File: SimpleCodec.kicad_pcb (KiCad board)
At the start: 4 copper layers, 0 parts

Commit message: Schematic
Updated the power delivery module.
Other minor changes.
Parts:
- added A1: RP_PICO_2, Custom_Parts:RP_PICO_2_THT, F.Cu at (18.0, 36.9)
- added C1: 10u, Capacitor_SMD:C_1206_3216Metric, F.Cu at (84.0, 15.0)
- added C10: 1u, Capacitor_SMD:C_0805_2012Metric, F.Cu at (67.7, 80.0)
- added C11: 2.2n, Capacitor_SMD:C_0603_1608Metric, F.Cu at (42.9, 81.7)
- added C12: 2.2n, Capacitor_SMD:C_0603_1608Metric, F.Cu at (42.9, 84.2)
- added C13: 10u, Capacitor_SMD:C_1206_3216Metric, F.Cu at (72.3, 55.9)
- added C14: 10u, Capacitor_SMD:C_1206_3216Metric, F.Cu at (72.3, 59.2)
- added C15: 4.7u, Capacitor_SMD:C_1206_3216Metric, F.Cu at (72.3, 62.5)
- added C16: 4.7u, Capacitor_SMD:C_1206_3216Metric, F.Cu at (72.3, 65.9)
- added C17: 100n, Capacitor_SMD:C_0603_1608Metric, F.Cu at (42.9, 86.8)
- added C18: 100n, Capacitor_SMD:C_0603_1608Metric, F.Cu at (47.0, 76.7)
- added C19: 4.7u, Capacitor_SMD:C_1206_3216Metric, F.Cu at (72.3, 15.0)
- added C2: 10u, Capacitor_SMD:C_1206_3216Metric, F.Cu at (84.0, 18.4)
- added C20: 4.7u, Capacitor_SMD:C_1206_3216Metric, F.Cu at (72.3, 18.4)
- added C21: 4.7u, Capacitor_SMD:C_1206_3216Metric, F.Cu at (72.3, 21.7)
- added C22: 4.7u, Capacitor_SMD:C_1206_3216Metric, F.Cu at (72.3, 25.1)
- added C23: 68p, Capacitor_SMD:C_0603_1608Metric, F.Cu at (42.9, 35.9)
- added C24: 68p, Capacitor_SMD:C_0603_1608Metric, F.Cu at (42.9, 38.4)
- added C25: 68p, Capacitor_SMD:C_0603_1608Metric, F.Cu at (42.9, 40.9)
- added C26: 68p, Capacitor_SMD:C_0603_1608Metric, F.Cu at (42.9, 43.4)
- added C27: 4.7u, Capacitor_SMD:C_1206_3216Metric, F.Cu at (72.3, 28.4)
- added C28: 4.7u, Capacitor_SMD:C_1206_3216Metric, F.Cu at (72.3, 31.8)
- added C29: 1n, Capacitor_SMD:C_0603_1608Metric, F.Cu at (42.9, 45.9)
- added C3: 10u, Capacitor_SMD:C_1206_3216Metric, F.Cu at (84.0, 21.7)
- added C30: 1n, Capacitor_SMD:C_0603_1608Metric, F.Cu at (42.9, 48.4)
- added C31: 100n, Capacitor_SMD:C_0603_1608Metric, F.Cu at (42.9, 50.9)
- added C32: 100n, Capacitor_SMD:C_0603_1608Metric, F.Cu at (47.0, 35.9)
- added C33: 4.7u, Capacitor_SMD:C_1206_3216Metric, F.Cu at (84.0, 55.9)
- added C34: 4.7u, Capacitor_SMD:C_1206_3216Metric, F.Cu at (84.0, 59.2)
- added C35: 100n, Capacitor_SMD:C_0603_1608Metric, F.Cu at (79.2, 55.4)
- added C36: 10u, Capacitor_SMD:C_1206_3216Metric, F.Cu at (84.0, 62.5)
- added C37: 1u, Capacitor_SMD:C_0805_2012Metric, F.Cu at (89.0, 62.0)
- added C38: 1u, Capacitor_SMD:C_0805_2012Metric, F.Cu at (89.0, 65.0)
- added C39: 10u, Capacitor_SMD:C_1206_3216Metric, F.Cu at (84.0, 65.9)
- added C4: 100n, Capacitor_SMD:C_0603_1608Metric, F.Cu at (79.2, 14.6)
- added C40: 100n, Capacitor_SMD:C_0603_1608Metric, F.Cu at (79.2, 57.9)
- added C41: 10u, Capacitor_SMD:C_1206_3216Metric, F.Cu at (84.0, 69.2)
- added C42: 100n, Capacitor_SMD:C_0603_1608Metric, F.Cu at (79.2, 60.5)
- added C7: 470p, Capacitor_SMD:C_0603_1608Metric, F.Cu at (42.9, 76.7)
- added C8: 470p, Capacitor_SMD:C_0603_1608Metric, F.Cu at (42.9, 79.2)
- added C9: 1u, Capacitor_SMD:C_0805_2012Metric, F.Cu at (67.7, 77.0)
- added J1: NMJ6HCD2, Custom_Parts:NMJ6HCD2_BORDER, F.Cu at (48.8, 56.7)
- added J2: NMJ6HCD2, Custom_Parts:NMJ6HCD2_BORDER, F.Cu at (48.8, 15.8)
- added Q1: AO3401A, Package_TO_SOT_SMD:SOT-23, F.Cu at (93.5, 25.6)
- added R1: 100K, Resistor_SMD:R_0603_1608Metric, F.Cu at (79.2, 17.1)
- added R10: 100K, Resistor_SMD:R_0603_1608Metric, F.Cu at (51.0, 79.2)
- added R11: 1K, Resistor_SMD:R_0603_1608Metric, F.Cu at (51.0, 81.7)
- added R12: 1K, Resistor_SMD:R_0603_1608Metric, F.Cu at (51.0, 84.2)
- added R13: 1K, Resistor_SMD:R_0603_1608Metric, F.Cu at (51.0, 86.8)
- added R14: 1K, Resistor_SMD:R_0603_1608Metric, F.Cu at (55.0, 76.7)
- added R15: 10K, Resistor_SMD:R_0603_1608Metric, F.Cu at (55.0, 79.2)
- added R16: 10K, Resistor_SMD:R_0603_1608Metric, F.Cu at (55.0, 81.7)
- added R17: 1K, Resistor_SMD:R_0603_1608Metric, F.Cu at (55.0, 84.2)
- added R18: 1K, Resistor_SMD:R_0603_1608Metric, F.Cu at (55.0, 86.8)
- added R19: 100K, Resistor_SMD:R_0603_1608Metric, F.Cu at (47.0, 38.4)
- added R2: 10K, Resistor_SMD:R_0603_1608Metric, F.Cu at (79.2, 19.6)
- added R20: 100K, Resistor_SMD:R_0603_1608Metric, F.Cu at (47.0, 40.9)
- added R21: 100K, Resistor_SMD:R_0603_1608Metric, F.Cu at (47.0, 43.4)
- added R22: 100K, Resistor_SMD:R_0603_1608Metric, F.Cu at (47.0, 45.9)
- added R23: 12K, Resistor_SMD:R_0603_1608Metric, F.Cu at (47.0, 48.4)
- added R24: 12K, Resistor_SMD:R_0603_1608Metric, F.Cu at (47.0, 50.9)
- added R25: 12K, Resistor_SMD:R_0603_1608Metric, F.Cu at (51.0, 35.9)
- added R26: 12K, Resistor_SMD:R_0603_1608Metric, F.Cu at (51.0, 38.4)
- added R27: 22K, Resistor_SMD:R_0603_1608Metric, F.Cu at (51.0, 40.9)
- added R28: 22K, Resistor_SMD:R_0603_1608Metric, F.Cu at (51.0, 43.4)
- added R29: 22K, Resistor_SMD:R_0603_1608Metric, F.Cu at (51.0, 45.9)
- added R3: 4.7K, Resistor_SMD:R_0603_1608Metric, F.Cu at (79.2, 22.1)
- added R30: 22K, Resistor_SMD:R_0603_1608Metric, F.Cu at (51.0, 48.4)
- added R31: 220, Resistor_SMD:R_0603_1608Metric, F.Cu at (51.0, 50.9)
- added R32: 220, Resistor_SMD:R_0603_1608Metric, F.Cu at (55.0, 35.9)
- added R33: 100, Resistor_SMD:R_0603_1608Metric, F.Cu at (55.0, 38.4)
- added R34: 100, Resistor_SMD:R_0603_1608Metric, F.Cu at (55.0, 40.9)
- added R35: 47K, Resistor_SMD:R_0603_1608Metric, F.Cu at (55.0, 43.4)
- added R36: 47K, Resistor_SMD:R_0603_1608Metric, F.Cu at (55.0, 45.9)
- added R37: 47K, Resistor_SMD:R_0603_1608Metric, F.Cu at (79.2, 63.0)
- added R38: 47K, Resistor_SMD:R_0603_1608Metric, F.Cu at (79.2, 65.5)
- added R39: 47K, Resistor_SMD:R_0603_1608Metric, F.Cu at (79.2, 68.0)
- added R4: 4.7K, Resistor_SMD:R_0603_1608Metric, F.Cu at (79.2, 24.6)
- added R40: 47K, Resistor_SMD:R_0603_1608Metric, F.Cu at (79.2, 70.5)
- added R41: 47K, Resistor_SMD:R_0603_1608Metric, F.Cu at (79.2, 73.0)
- added R42: 47K, Resistor_SMD:R_0603_1608Metric, F.Cu at (79.2, 75.5)
- added R5: 100, Resistor_SMD:R_0603_1608Metric, F.Cu at (47.0, 79.2)
- added R6: 100, Resistor_SMD:R_0603_1608Metric, F.Cu at (47.0, 81.7)
- added R7: 100K, Resistor_SMD:R_0603_1608Metric, F.Cu at (47.0, 84.2)
- added R8: 100K, Resistor_SMD:R_0603_1608Metric, F.Cu at (47.0, 86.8)
- added R9: 100K, Resistor_SMD:R_0603_1608Metric, F.Cu at (51.0, 76.7)
- added U1: NE5532, Package_SO:SOIC-8_3.9x4.9mm_P1.27mm, F.Cu at (91.0, 16.7)
- added U3: AMS1117-3.3, Package_TO_SOT_SMD:SOT-223-3_TabPin2, F.Cu at (86.1, 27.6)
- added U4: NE5532, Package_SO:SOIC-8_3.9x4.9mm_P1.27mm, F.Cu at (61.2, 78.8)
- added U5: NE5532, Package_SO:SOIC-8_3.9x4.9mm_P1.27mm, F.Cu at (61.2, 85.4)
- added U6: NE5532, Package_SO:SOIC-8_3.9x4.9mm_P1.27mm, F.Cu at (61.2, 38.0)
- added U7: NE5532, Package_SO:SOIC-8_3.9x4.9mm_P1.27mm, F.Cu at (61.2, 44.5)
- added U8: TAC5242, Custom_Parts:VQFN-24-1EP_4x4mm_P0.5mm_EP2.1x2.1mm_ThermalVias, F.Cu at (90.0, 57.3)

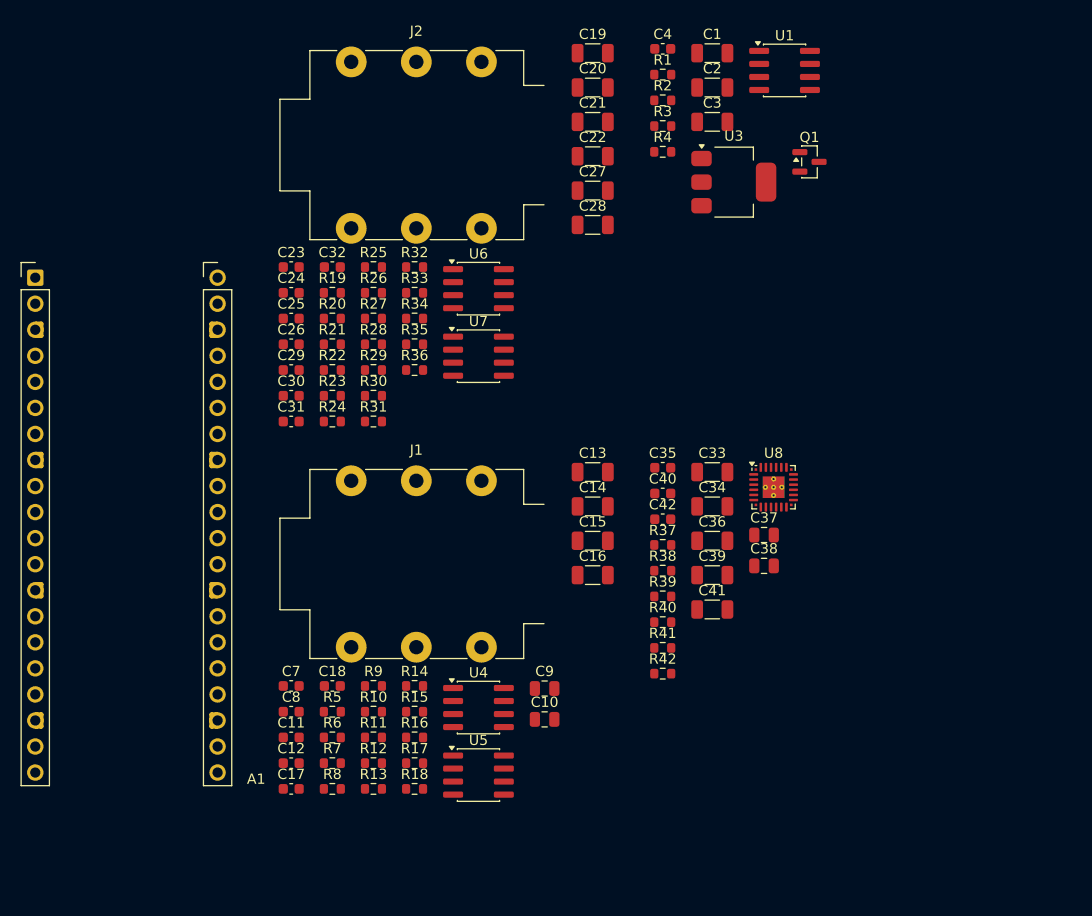
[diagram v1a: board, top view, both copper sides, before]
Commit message: Moved to a CS4272 codec as a cheaper alternative with similar performance.
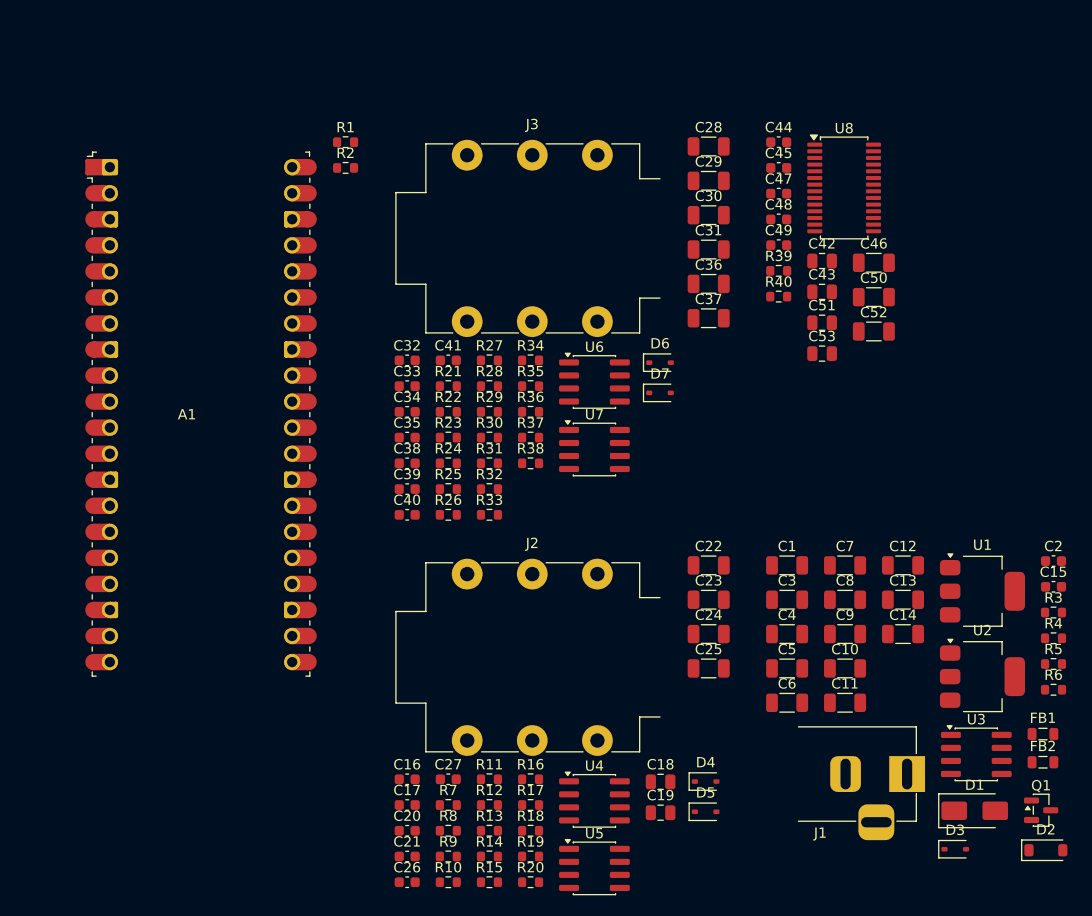
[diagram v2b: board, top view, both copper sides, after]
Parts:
- removed R41, R42: 47K, Resistor_SMD:R_0603_1608Metric
- added C43: 1u, Capacitor_SMD:C_0805_2012Metric, F.Cu at (94.7, 38.3)
- added C44: 100n, Capacitor_SMD:C_0603_1608Metric, F.Cu at (90.5, 23.7)
- added C45: 100n, Capacitor_SMD:C_0603_1608Metric, F.Cu at (90.5, 26.2)
- added C46: 4.7u, Capacitor_SMD:C_1206_3216Metric, F.Cu at (99.8, 35.4)
- added C47: 100n, Capacitor_SMD:C_0603_1608Metric, F.Cu at (90.5, 28.7)
- added C48: 100n, Capacitor_SMD:C_0603_1608Metric, F.Cu at (90.5, 31.2)
- added C49: 100n, Capacitor_SMD:C_0603_1608Metric, F.Cu at (90.5, 33.7)
- added C5: 10u, Capacitor_SMD:C_1206_3216Metric, F.Cu at (91.3, 75.0)
- added C50: 4.7u, Capacitor_SMD:C_1206_3216Metric, F.Cu at (99.8, 38.8)
- added C51: 1u, Capacitor_SMD:C_0805_2012Metric, F.Cu at (94.7, 41.3)
- added C52: 22u, Capacitor_SMD:C_1206_3216Metric, F.Cu at (99.8, 42.1)
- added C53: 1u, Capacitor_SMD:C_0805_2012Metric, F.Cu at (94.7, 44.3)
- added C6: 4.7u, Capacitor_SMD:C_1206_3216Metric, F.Cu at (91.3, 78.3)
- added D1: SMAJ10CA, Diode_SMD:D_SMA, F.Cu at (109.6, 88.9)
- added D2: MMSZ5248B, Diode_SMD:D_SOD-123, F.Cu at (116.5, 92.7)
- added D3: 1N5819WS, Diode_SMD:D_SOD-323, F.Cu at (107.7, 92.6)
- added D4: H15VSD3B, Diode_SMD:D_SOD-323, F.Cu at (83.4, 86.0)
- added D5: H15VSD3B, Diode_SMD:D_SOD-323, F.Cu at (83.4, 89.0)
- added D6: H15VSD3B, Diode_SMD:D_SOD-323, F.Cu at (78.9, 45.2)
- added D7: H15VSD3B, Diode_SMD:D_SOD-323, F.Cu at (78.9, 48.1)
- added FB1: 300, Inductor_SMD:L_0805_2012Metric, F.Cu at (116.2, 81.4)
- added FB2: 300, Inductor_SMD:L_0805_2012Metric, F.Cu at (116.2, 84.2)
- added J3: NMJ6HCD2, Custom_Parts:NMJ6HCD2_BORDER, F.Cu at (60.1, 24.9)
- added U2: AMS1117-3.3, Package_TO_SOT_SMD:SOT-223-3_TabPin2, F.Cu at (110.3, 75.8)
- A1: footprint Custom_Parts:RP_PICO_2_THT -> Custom_Parts:RP_PICO_2_SMD
- C1, C13, C3: value 10u -> 22u
- C10, C37, C9: value 1u -> 4.7u; footprint Capacitor_SMD:C_0805_2012Metric -> Capacitor_SMD:C_1206_3216Metric
- C11: value 2.2n -> 10u; footprint Capacitor_SMD:C_0603_1608Metric -> Capacitor_SMD:C_1206_3216Metric
- C12: value 2.2n -> 22u; footprint Capacitor_SMD:C_0603_1608Metric -> Capacitor_SMD:C_1206_3216Metric
- C15, C27: value 4.7u -> 100n; footprint Capacitor_SMD:C_1206_3216Metric -> Capacitor_SMD:C_0603_1608Metric
- C16: value 4.7u -> 470p; footprint Capacitor_SMD:C_1206_3216Metric -> Capacitor_SMD:C_0603_1608Metric
- C17: value 100n -> 470p
- C18, C42: value 100n -> 1u; footprint Capacitor_SMD:C_0603_1608Metric -> Capacitor_SMD:C_0805_2012Metric
- C19: value 4.7u -> 1u; footprint Capacitor_SMD:C_1206_3216Metric -> Capacitor_SMD:C_0805_2012Metric
- C2: value 10u -> 10n; footprint Capacitor_SMD:C_1206_3216Metric -> Capacitor_SMD:C_0603_1608Metric
- C20, C21: value 4.7u -> 2.2n; footprint Capacitor_SMD:C_1206_3216Metric -> Capacitor_SMD:C_0603_1608Metric
- C22: value 4.7u -> 10u
- C23: value 68p -> 10u; footprint Capacitor_SMD:C_0603_1608Metric -> Capacitor_SMD:C_1206_3216Metric
- C24, C25: value 68p -> 4.7u; footprint Capacitor_SMD:C_0603_1608Metric -> Capacitor_SMD:C_1206_3216Metric
- C26: value 68p -> 100n
- C29, C30: value 1n -> 4.7u; footprint Capacitor_SMD:C_0603_1608Metric -> Capacitor_SMD:C_1206_3216Metric
- C31, C4: value 100n -> 4.7u; footprint Capacitor_SMD:C_0603_1608Metric -> Capacitor_SMD:C_1206_3216Metric
- C32, C35: value 100n -> 68p
- C33, C34: value 4.7u -> 68p; footprint Capacitor_SMD:C_1206_3216Metric -> Capacitor_SMD:C_0603_1608Metric
- C36: value 10u -> 4.7u
- C38: value 1u -> 1n; footprint Capacitor_SMD:C_0805_2012Metric -> Capacitor_SMD:C_0603_1608Metric
- C39: value 10u -> 1n; footprint Capacitor_SMD:C_1206_3216Metric -> Capacitor_SMD:C_0603_1608Metric
- C41: value 10u -> 100n; footprint Capacitor_SMD:C_1206_3216Metric -> Capacitor_SMD:C_0603_1608Metric
- C7, C8: value 470p -> 10u; footprint Capacitor_SMD:C_0603_1608Metric -> Capacitor_SMD:C_1206_3216Metric
- J1: value NMJ6HCD2 -> DC-005-2.5A-2.0; footprint Custom_Parts:NMJ6HCD2_BORDER -> Custom_Parts:BARREL_JACK_HORIZONTAL
- R1: value 100K -> 47K
- R11, R12: value 1K -> 100K
- R15, R16: value 10K -> 1K
- R17, R18: value 1K -> 10K
- R19, R20: value 100K -> 1K
- R2: value 10K -> 47K
- R23, R24: value 12K -> 100K
- R27, R28: value 22K -> 12K
- R31, R32: value 220 -> 22K
- R33, R34: value 100 -> 220
- R35, R36: value 47K -> 100
- R4: value 4.7K -> 100
- R5, R6: value 100 -> 4.7K
- R7, R8: value 100K -> 100
- U1: value NE5532 -> AMS1117-5.0; footprint Package_SO:SOIC-8_3.9x4.9mm_P1.27mm -> Package_TO_SOT_SMD:SOT-223-3_TabPin2
- U3: value AMS1117-3.3 -> NE5532; footprint Package_TO_SOT_SMD:SOT-223-3_TabPin2 -> Package_SO:SOIC-8_3.9x4.9mm_P1.27mm
- U8: value TAC5242 -> CS4272; footprint Custom_Parts:VQFN-24-1EP_4x4mm_P0.5mm_EP2.1x2.1mm_ThermalVias -> Package_SO:TSSOP-28_4.4x9.7mm_P0.65mm
- moved C20 74.7 mm to (54.2, 90.8)
- moved C19 74.4 mm to (79.0, 89.1)
- moved C21 73.9 mm to (54.2, 93.3)
- moved R5 70.5 mm to (117.3, 74.6)
- moved R6 70.5 mm to (117.3, 77.1)
- moved Q1 67.1 mm to (116.1, 88.8)
- moved C12 62.7 mm to (102.6, 65.0)
- moved J1 61.3 mm to (103.0, 85.3)
- moved R3 60.9 mm to (117.3, 69.5)
- moved R4 60.9 mm to (117.3, 72.1)
- moved U3 60.6 mm to (109.8, 83.4)
- moved C27 59.1 mm to (58.3, 85.8)
- moved C4 58.3 mm to (91.3, 71.7)
- moved R19 58.3 mm to (66.3, 93.3)
- moved R20 58.3 mm to (66.3, 95.8)
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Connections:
- net I2S_DOUT renamed I2S_LRCK
- A1 pad 14: MD0 -> unconnected-(A1-GPIO10-Pad14)
- A1 pad 15: MD1 -> unconnected-(A1-GPIO11-Pad15)
- A1 pad 16: MD2 -> I2C_SDA
- A1 pad 17: MD3 -> I2C_SCL
- A1 pad 19: MD4 -> unconnected-(A1-GPIO14-Pad19)_1
- A1 pad 20: MD5 -> unconnected-(A1-GPIO15-Pad20)
- A1 pad 21: I2S_DIN -> I2S_MCLK
- A1 pad 24: I2S_FSYNC -> I2S_SCLK
- A1 pad 25: I2S_BCLK -> I2S_SDOUT
- A1 pad 26: unconnected-(A1-GPIO20-Pad26) -> I2S_SDIN
- A1 pad 27: CLK_INT -> unconnected-(A1-GPIO21-Pad27)_1
- A1 pad 29: unconnected-(A1-GPIO22-Pad29) -> CODEC_RST
- A1 pad 36: +3V3 -> unconnected-(A1-3V3-Pad36)_1
- A1 pad 39: unconnected-(A1-VSYS-Pad39) -> +VSYS
- A1 pad 40: +5V -> unconnected-(A1-VBUS-Pad40)
- A1 pad 6: +3V3D -> unconnected-(A1-GPIO4-Pad6)_1
- A1 pad 7: 3V3A_EN -> unconnected-(A1-GPIO5-Pad7)
- C1 pad 1: /Power/VBIAS_RAW -> +VCC_FILT
- C10 pad 1: Net-(C10-Pad1) -> +5VA
- C10 pad 2: Net-(U5A-+) -> GND
- C11 pad 1: Net-(C11-Pad1) -> +3V3D
- C12 pad 1: Net-(C12-Pad1) -> +5VA
- C13 pad 1: Net-(C11-Pad1) -> +5VA
- C13 pad 2: Net-(U4B-+) -> GND
- C14 pad 1: Net-(C12-Pad1) -> /Power/+VBIAS_RAW
- C14 pad 2: Net-(U5B-+) -> GND
- C15 pad 1: Net-(U4B--) -> +VCC_FILT
- C15 pad 2: Net-(C15-Pad2) -> GND
- C16 pad 1: Net-(U5B--) -> Net-(C16-Pad1)
- C16 pad 2: Net-(C16-Pad2) -> GND
- C17 pad 1: +3V3A -> Net-(C17-Pad1)
- C18 pad 1: +3V3A -> Net-(C16-Pad1)
- C18 pad 2: GND -> Net-(U4A-+)
- C19 pad 1: CODEC_OUTL- -> Net-(C17-Pad1)
- C19 pad 2: Net-(C19-Pad2) -> Net-(U5A-+)
- C2 pad 1: +5V_EN -> /Power/PROT_G
- C20 pad 1: CODEC_OUTL+ -> Net-(C20-Pad1)
- C20 pad 2: Net-(C20-Pad2) -> GND
- C21 pad 1: CODEC_OUTR- -> Net-(C21-Pad1)
- C21 pad 2: Net-(C21-Pad2) -> GND
- C22 pad 1: CODEC_OUTR+ -> Net-(C20-Pad1)
- C22 pad 2: Net-(C22-Pad2) -> Net-(U4B-+)
- C23 pad 1: Net-(U6A--) -> Net-(C21-Pad1)
- C23 pad 2: Net-(C23-Pad2) -> Net-(U5B-+)
- C24 pad 1: Net-(U7A--) -> Net-(U4B--)
- C25 pad 1: Net-(U6A-+) -> Net-(U5B--)
- C25 pad 2: VBIAS_OUT -> Net-(C25-Pad2)
- C26 pad 1: Net-(U7A-+) -> +VCC_FILT
- C26 pad 2: VBIAS_OUT -> GND
- C27 pad 1: Net-(U6B--) -> +VCC_FILT
- C27 pad 2: Net-(C27-Pad2) -> GND
- C28 pad 1: Net-(U7B--) -> CODEC_OUTL-
- C29 pad 1: /Buffers_Out/AUDIO_OUTL -> CODEC_OUTL+
- C29 pad 2: GND -> Net-(C29-Pad2)
- C3 pad 1: +3V3A -> +VCC_FILT
- C30 pad 1: /Buffers_Out/AUDIO_OUTR -> CODEC_OUTR-
- C30 pad 2: GND -> Net-(C30-Pad2)
- C31 pad 1: +3V3A -> CODEC_OUTR+
- C31 pad 2: GND -> Net-(C31-Pad2)
- C32 pad 1: +3V3A -> Net-(U6A--)
- C32 pad 2: GND -> Net-(C32-Pad2)
- C33 pad 1: /Codec/INLM -> Net-(U7A--)
- C33 pad 2: GND -> Net-(C33-Pad2)
- C34 pad 1: /Codec/INRM -> Net-(U6A-+)
- C34 pad 2: GND -> VBIAS_OUT
- C35 pad 1: +3V3A -> Net-(U7A-+)
- C35 pad 2: GND -> VBIAS_OUT
- C36 pad 1: +3V3A -> Net-(U6B--)
- C36 pad 2: GND -> Net-(C36-Pad2)
- C37 pad 1: Net-(U8-MICBIAS) -> Net-(U7B--)
- C37 pad 2: GND -> Net-(C37-Pad2)
- C38 pad 1: /Codec/VREF -> /Buffers_Out/AUDIO_OUTL
- C39 pad 1: /Codec/DREG -> /Buffers_Out/AUDIO_OUTR
- C4 pad 1: +3V3A -> +VDC_PROT
- C40 pad 1: /Codec/DREG -> +VCC_FILT
- C41 pad 1: +3V3D -> +VCC_FILT
- C42 pad 1: +3V3D -> GND
- C42 pad 2: GND -> +3V3D
- C7 pad 1: Net-(C7-Pad1) -> +5VA_RAW
- C8 pad 1: Net-(C10-Pad1) -> +VCC
- C9 pad 1: Net-(C7-Pad1) -> +5VA_RAW
- C9 pad 2: Net-(U4A-+) -> GND
- J2 pad R: /Buffers_Out/AUDIO_OUTR -> /Buffers_In/AUDIO_INR
- J2 pad T: /Buffers_Out/AUDIO_OUTL -> /Buffers_In/AUDIO_INL
- Q1 pad 1: /Power/GATE_EN -> /Power/PROT_G
- Q1 pad 2: +5V -> +VDC_PROT
- Q1 pad 3: +5V_EN -> +VDC
- R1 pad 1: +3V3 -> +3V3D
- R1 pad 2: /Power/GATE_EN -> I2C_SDA
- R10 pad 1: Net-(U5A-+) -> GND
- R10 pad 2: VBIAS_IN -> Net-(C17-Pad1)
- R11 pad 1: Net-(U4A--) -> Net-(U4A-+)
- R11 pad 2: Net-(C11-Pad1) -> +VBIAS_IN
- R12 pad 1: Net-(U5A--) -> Net-(U5A-+)
- R12 pad 2: Net-(C12-Pad1) -> +VBIAS_IN
- R13 pad 1: GND -> Net-(U4A--)
- R13 pad 2: Net-(C11-Pad1) -> Net-(C20-Pad1)
- R14 pad 1: GND -> Net-(U5A--)
- R14 pad 2: Net-(C12-Pad1) -> Net-(C21-Pad1)
- R15 pad 1: Net-(U4B-+) -> GND
- R15 pad 2: VBIAS_IN -> Net-(C20-Pad1)
- R16 pad 1: Net-(U5B-+) -> GND
- R16 pad 2: VBIAS_IN -> Net-(C21-Pad1)
- R17 pad 1: Net-(C15-Pad2) -> Net-(U4B-+)
- R17 pad 2: CODEC_INL -> VBIAS_IN
- R18 pad 1: Net-(C16-Pad2) -> Net-(U5B-+)
- R18 pad 2: CODEC_INR -> VBIAS_IN
- R19 pad 1: VBIAS_OUT -> Net-(C24-Pad2)
- R19 pad 2: Net-(C19-Pad2) -> CODEC_INL
- R2 pad 1: /Power/GATE_EN -> +3V3D
- R2 pad 2: 3V3A_EN -> I2C_SCL
- R20 pad 1: Net-(C20-Pad2) -> Net-(C25-Pad2)
- R20 pad 2: VBIAS_OUT -> CODEC_INR
- R21 pad 1: VBIAS_OUT -> +VBIAS_OUT
- R21 pad 2: Net-(C21-Pad2) -> Net-(C28-Pad2)
- R22 pad 1: Net-(C22-Pad2) -> Net-(C29-Pad2)
- R23 pad 1: Net-(C19-Pad2) -> +VBIAS_OUT
- R23 pad 2: Net-(U6A--) -> Net-(C30-Pad2)
- R24 pad 1: Net-(C20-Pad2) -> Net-(C31-Pad2)
- R24 pad 2: Net-(U6A-+) -> VBIAS_OUT
- R25 pad 1: Net-(C21-Pad2) -> Net-(C28-Pad2)
- R25 pad 2: Net-(U7A--) -> Net-(U6A--)
- R26 pad 1: Net-(C22-Pad2) -> Net-(C29-Pad2)
- R26 pad 2: Net-(U7A-+) -> Net-(U6A-+)
- R27 pad 1: Net-(U6A-+) -> Net-(C30-Pad2)
- R27 pad 2: VBIAS_OUT -> Net-(U7A--)
- R28 pad 1: Net-(U7A-+) -> Net-(C31-Pad2)
- R28 pad 2: VBIAS_OUT -> Net-(U7A-+)
- R29 pad 1: Net-(U6A--) -> Net-(U6A-+)
- R29 pad 2: Net-(C23-Pad2) -> VBIAS_OUT
- R3 pad 1: +3V3A -> /Power/PROT_G
- R3 pad 2: /Power/VBIAS_RAW -> GND
- R30 pad 1: Net-(U7A--) -> Net-(U7A-+)
- R30 pad 2: Net-(C24-Pad2) -> VBIAS_OUT
- R31 pad 1: Net-(C23-Pad2) -> Net-(U6A--)
- R31 pad 2: Net-(U6B-+) -> Net-(C32-Pad2)
- R32 pad 1: Net-(C24-Pad2) -> Net-(U7A--)
- R32 pad 2: Net-(U7B-+) -> Net-(C33-Pad2)
- R33 pad 1: Net-(C27-Pad2) -> Net-(C32-Pad2)
- R33 pad 2: /Buffers_Out/AUDIO_OUTL -> Net-(U6B-+)
- R34 pad 1: Net-(C28-Pad2) -> Net-(C33-Pad2)
- R34 pad 2: /Buffers_Out/AUDIO_OUTR -> Net-(U7B-+)
- R35 pad 1: /Buffers_Out/AUDIO_OUTL -> Net-(C36-Pad2)
- R35 pad 2: GND -> /Buffers_Out/AUDIO_OUTL
- R36 pad 1: /Buffers_Out/AUDIO_OUTR -> Net-(C37-Pad2)
- R36 pad 2: GND -> /Buffers_Out/AUDIO_OUTR
- R37 pad 1: MD0 -> /Buffers_Out/AUDIO_OUTL
- R38 pad 1: MD1 -> /Buffers_Out/AUDIO_OUTR
- R39 pad 1: MD2 -> Net-(U8-~{BMUTEC})
- R4 pad 1: /Power/VBIAS_RAW -> +VCC
- R4 pad 2: GND -> +VCC_FILT
- R40 pad 1: MD3 -> Net-(U8-~{AMUTEC})
- R5 pad 1: /Buffers_In/AUDIO_INL -> +VCC_FILT
- R5 pad 2: Net-(C7-Pad1) -> /Power/+VBIAS_RAW
- R6 pad 1: /Buffers_In/AUDIO_INR -> /Power/+VBIAS_RAW
- R6 pad 2: Net-(C10-Pad1) -> GND
- R7 pad 1: GND -> /Buffers_In/AUDIO_INL
- R7 pad 2: Net-(C7-Pad1) -> Net-(C16-Pad1)
- R8 pad 1: GND -> /Buffers_In/AUDIO_INR
- R8 pad 2: Net-(C10-Pad1) -> Net-(C17-Pad1)
- R9 pad 1: Net-(U4A-+) -> GND
- R9 pad 2: VBIAS_IN -> Net-(C16-Pad1)
- U1 pad 1: VBIAS_IN -> GND
- U1 pad 2: VBIAS_IN -> +5VA_RAW
- U1 pad 3: /Power/VBIAS_RAW -> +VCC_FILT
- U3 pad 1: GND -> +VBIAS_IN
- U3 pad 2: +3V3A -> +VBIAS_IN
- U3 pad 3: +5V_EN -> /Power/+VBIAS_RAW
- U4 pad 8: +3V3A -> +VCC_FILT
- U5 pad 8: +3V3A -> +VCC_FILT
- U6 pad 1: Net-(C23-Pad2) -> Net-(C32-Pad2)
- U6 pad 8: +3V3A -> +VCC_FILT
- U7 pad 1: Net-(C24-Pad2) -> Net-(C33-Pad2)
- U7 pad 8: +3V3A -> +VCC_FILT
- U8 pad 1: /Codec/DREG -> unconnected-(U8-XT0-Pad1)
- U8 pad 10: MD4 -> +3V3D
- U8 pad 11: CLK_INT -> I2C_SCL
- U8 pad 12: MD5 -> I2C_SDA
- U8 pad 13: MD0 -> GND
- U8 pad 14: Net-(U8-MICBIAS) -> CODEC_RST
- U8 pad 15: CODEC_INL -> /Codec/VCOM
- U8 pad 16: /Codec/INLM -> /Codec/INL-
- U8 pad 17: CODEC_INR -> CODEC_INL
- U8 pad 18: /Codec/INRM -> CODEC_INR
- U8 pad 19: CODEC_OUTL- -> /Codec/INR-
- U8 pad 2: I2S_BCLK -> unconnected-(U8-XTI-Pad2)
- U8 pad 20: CODEC_OUTL+ -> +5VA
- U8 pad 21: CODEC_OUTR+ -> GND
- U8 pad 22: CODEC_OUTR- -> /Codec/VFILT+
- U8 pad 23: +3V3A -> Net-(U8-~{AMUTEC})
- U8 pad 24: /Codec/VREF -> CODEC_OUTL-
- U8 pad 25: GND -> CODEC_OUTL+
- U8 pad 3: I2S_FSYNC -> I2S_MCLK
- U8 pad 5: I2S_DIN -> I2S_SCLK
- U8 pad 6: +3V3D -> I2S_SDOUT
- U8 pad 7: MD1 -> I2S_SDIN
- U8 pad 8: MD2 -> GND
- U8 pad 9: MD3 -> +3V3D
